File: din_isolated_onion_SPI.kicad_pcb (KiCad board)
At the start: 2 copper layers, 32.5 x 40.5 mm, 17 parts, among them J1 Conn_01x16, J2 Conn_01x16, J3 Conn_01x10, U1 Omega2+, U2 SI8661AB-B-IS1

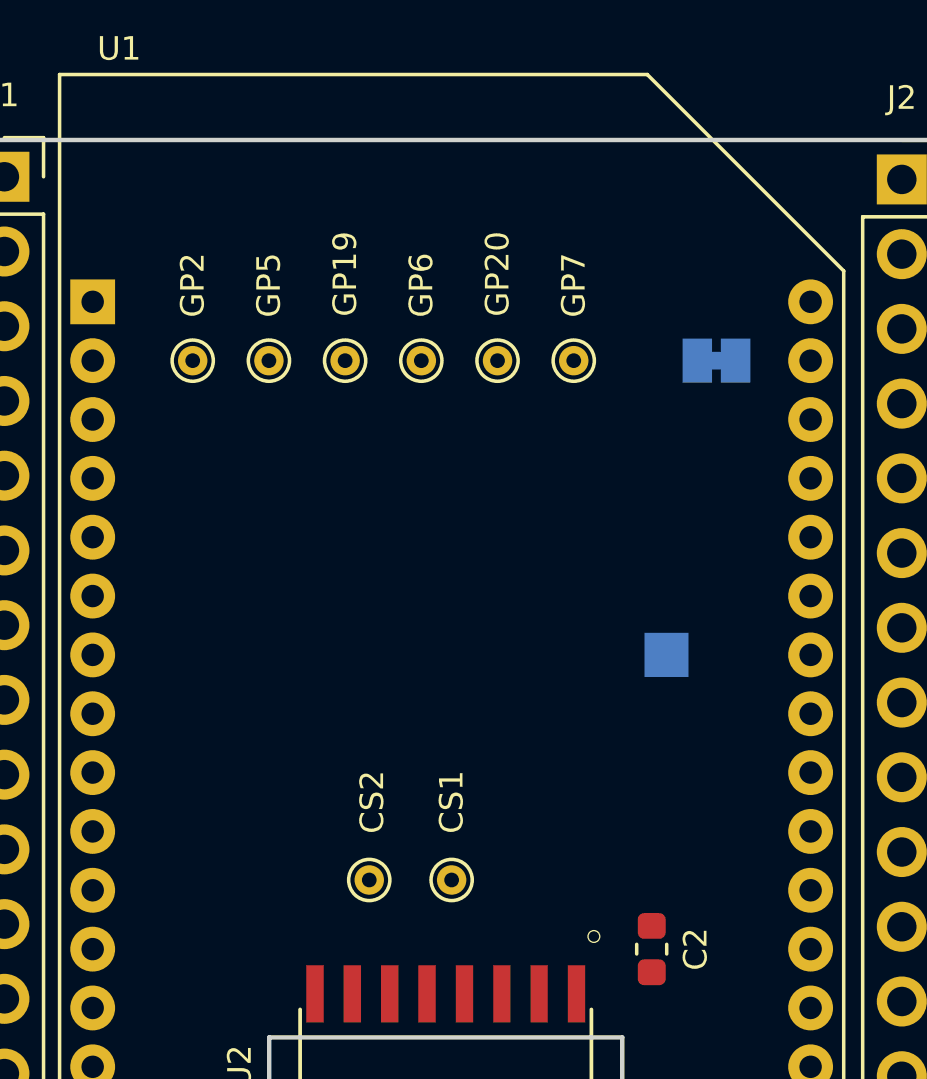
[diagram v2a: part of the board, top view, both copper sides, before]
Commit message: Add reset IC and finalize test points
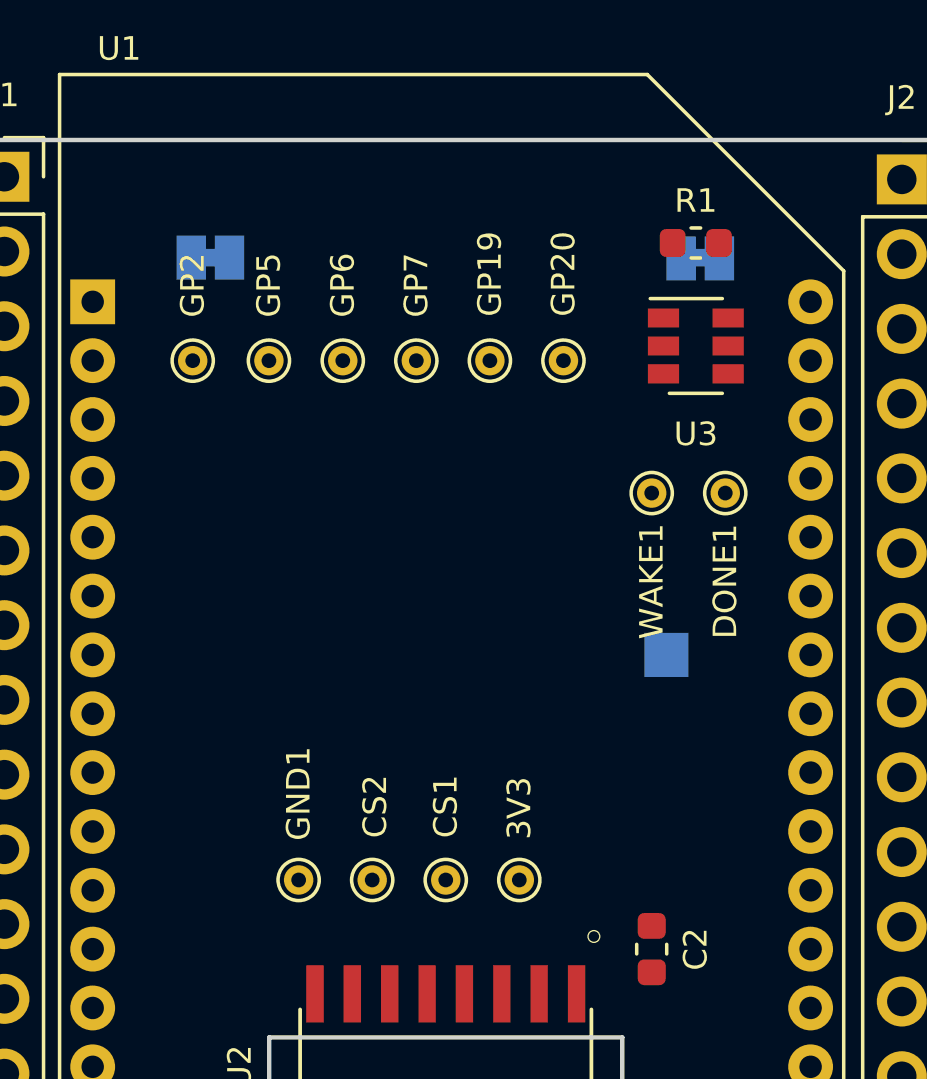
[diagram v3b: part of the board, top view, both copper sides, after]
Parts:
- removed JP1: Jumper_2_Bridged, Jumper:SolderJumper-2_P1.3mm_Bridged_Pad1.0x1.5mm
- added 3V3: TestPoint, TestPoint:TestPoint_THTPad_D1.0mm_Drill0.5mm, F.Cu at (148.5, 104.7)
- added DONE1: TestPoint, TestPoint:TestPoint_THTPad_D1.0mm_Drill0.5mm, F.Cu at (155.5, 91.5)
- added GND1: GND, TestPoint:TestPoint_THTPad_D1.0mm_Drill0.5mm, F.Cu at (141.0, 104.7)
- added LOGO1: Logo_Open_Hardware_Large, Symbol:OSHW-Logo2_7.3x6mm_SilkScreen, B.Cu at (145.0, 100.0)
- added R1: 29.4K, Resistor_SMD:R_0603_1608Metric, F.Cu at (154.5, 83.0)
- added RST1: Jumper_2_Bridged, Jumper:SolderJumper-2_P1.3mm_Bridged_Pad1.0x1.5mm, B.Cu at (154.7, 83.5)
- added U3: TPL5010-Q1, Package_TO_SOT_SMD:SOT-23-6, F.Cu at (154.5, 86.5)
- added VCC1: Jumper_2_Bridged, Jumper:SolderJumper-2_P1.3mm_Bridged_Pad1.0x1.5mm, B.Cu at (138.0, 83.5)
- added WAKE1: TestPoint, TestPoint:TestPoint_THTPad_D1.0mm_Drill0.5mm, F.Cu at (153.0, 91.5)
- CS1: value TestPoint -> ChipSel1
- CS2: value TestPoint -> ChipSel2
- moved GP7 5.35 mm to (145.0, 87.0)
- moved GP19 4.92 mm to (147.5, 87.0)
- moved GP6 2.67 mm to (142.5, 87.0)
- moved GP20 2.24 mm to (150.0, 87.0)
- moved CS1 0.20 mm to (146.0, 104.7)
- moved CS2 0.10 mm to (143.5, 104.7)
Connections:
- net Net-(J2-Pad1) renamed ~RST
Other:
- board text added: "DIN Onion SPI Isolator http://whatnick.com v0.1 2019-06-20"

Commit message: Finalize v0.1 routing
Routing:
- net 3V3_C: track 0.00 -> 103.7 mm, vias 0 -> 1
- net GND_C: track 0.00 -> 94.3 mm, vias 0 -> 5
- net Net-(GP19-Pad1): track 0.00 -> 76.1 mm, vias 0 -> 1
- net Net-(GP20-Pad1): track 0.00 -> 73.2 mm
- net Net-(J2-Pad6): track 0.00 -> 59.4 mm
- net Net-(J2-Pad7): track 0.00 -> 58.4 mm, vias 0 -> 1
- net ~RST: track 0.00 -> 51.4 mm
- net 3V3_O: track 0.00 -> 46.0 mm
- net GND_I: track 0.00 -> 31.8 mm, vias 0 -> 1
- net 3V3_I: track 0.00 -> 31.7 mm
- net CS0_O: track 0.00 -> 20.6 mm
- net CLK_O: track 0.00 -> 20.3 mm
- net Net-(GP7-Pad1): track 0.00 -> 20.3 mm
- net Net-(GP6-Pad1): track 0.00 -> 17.2 mm
- net MOSI_O: track 0.00 -> 16.4 mm, vias 0 -> 1
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- added copper zone on B.Cu, net GND_C
- added copper zone on F.Cu, net GND_C
- added copper zone on B.Cu, net GND_I
- added copper zone on F.Cu, net GND_I

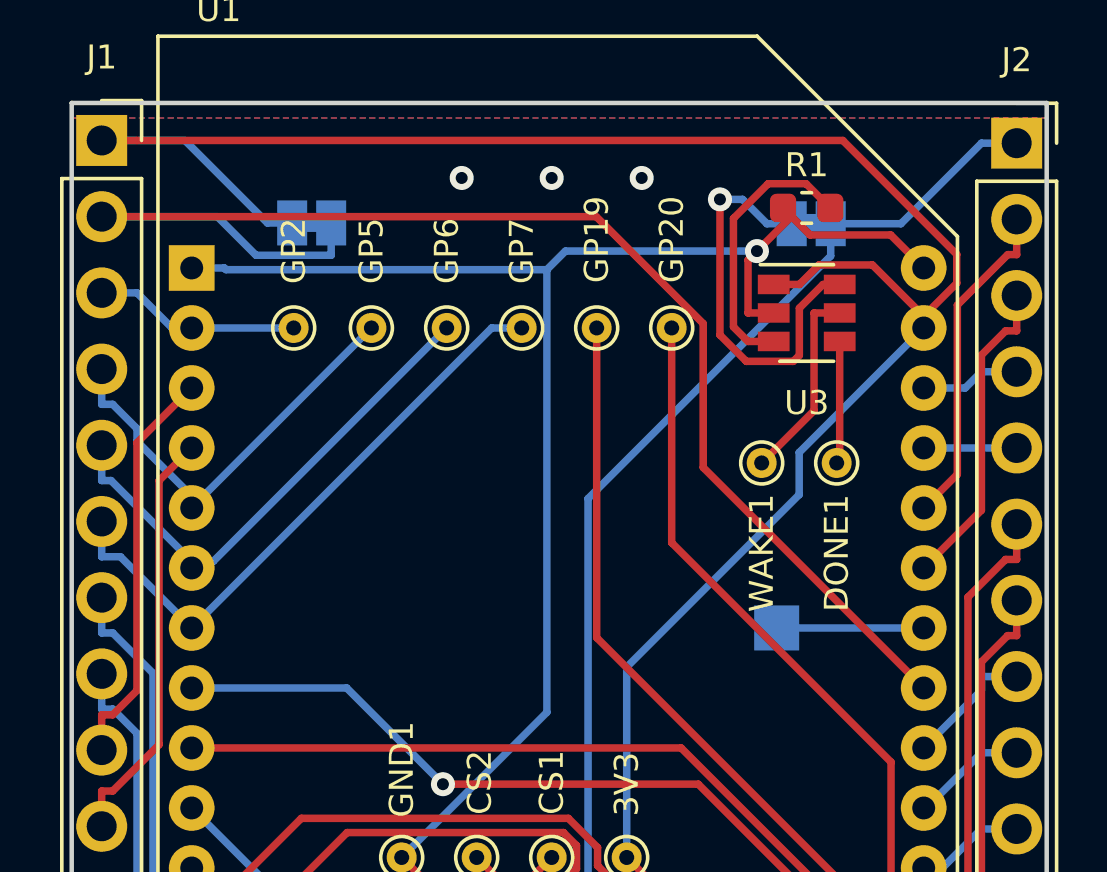
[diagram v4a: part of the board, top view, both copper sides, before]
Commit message: Switch to TSOT for hardware reset
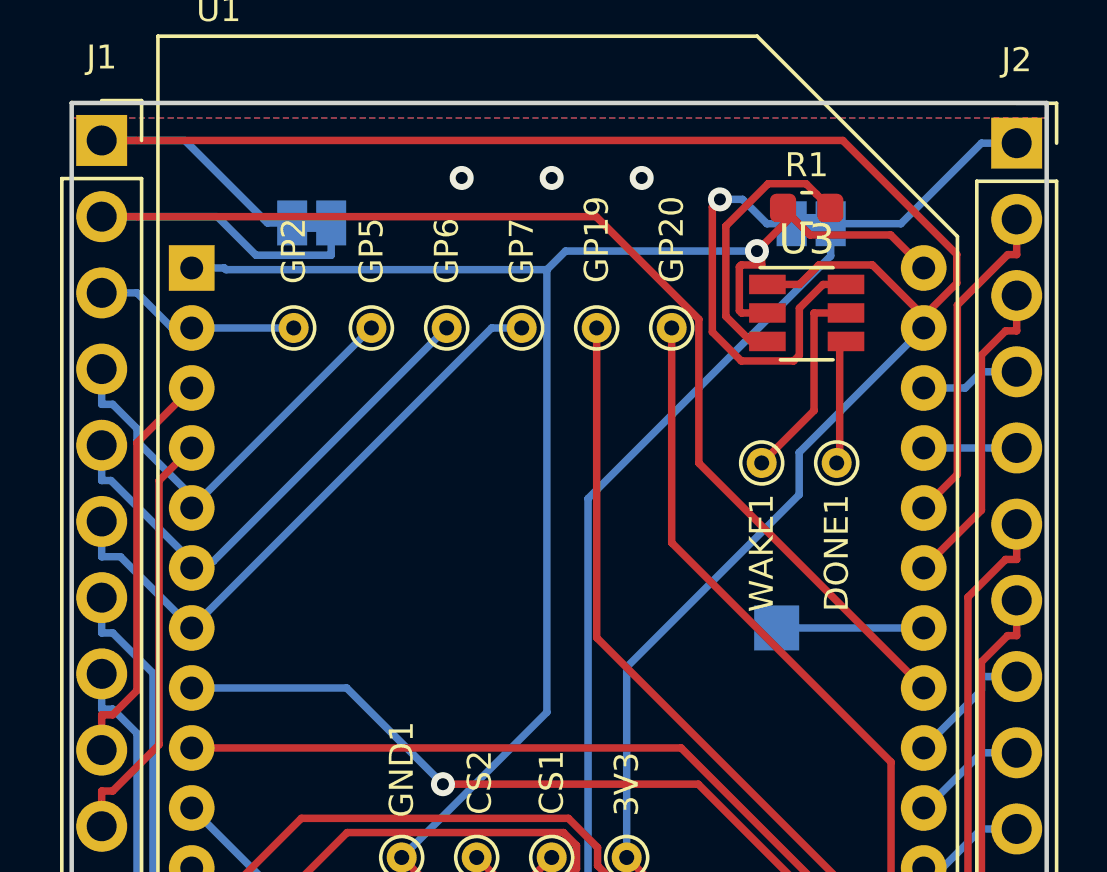
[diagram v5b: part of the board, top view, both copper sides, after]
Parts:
- C1, C2: value C_Small -> 100nF
- U3: footprint Package_TO_SOT_SMD:SOT-23-6 -> Package_TO_SOT_SMD:TSOT-23-6
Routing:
- net GND_C: track 94.3 -> 95.4 mm

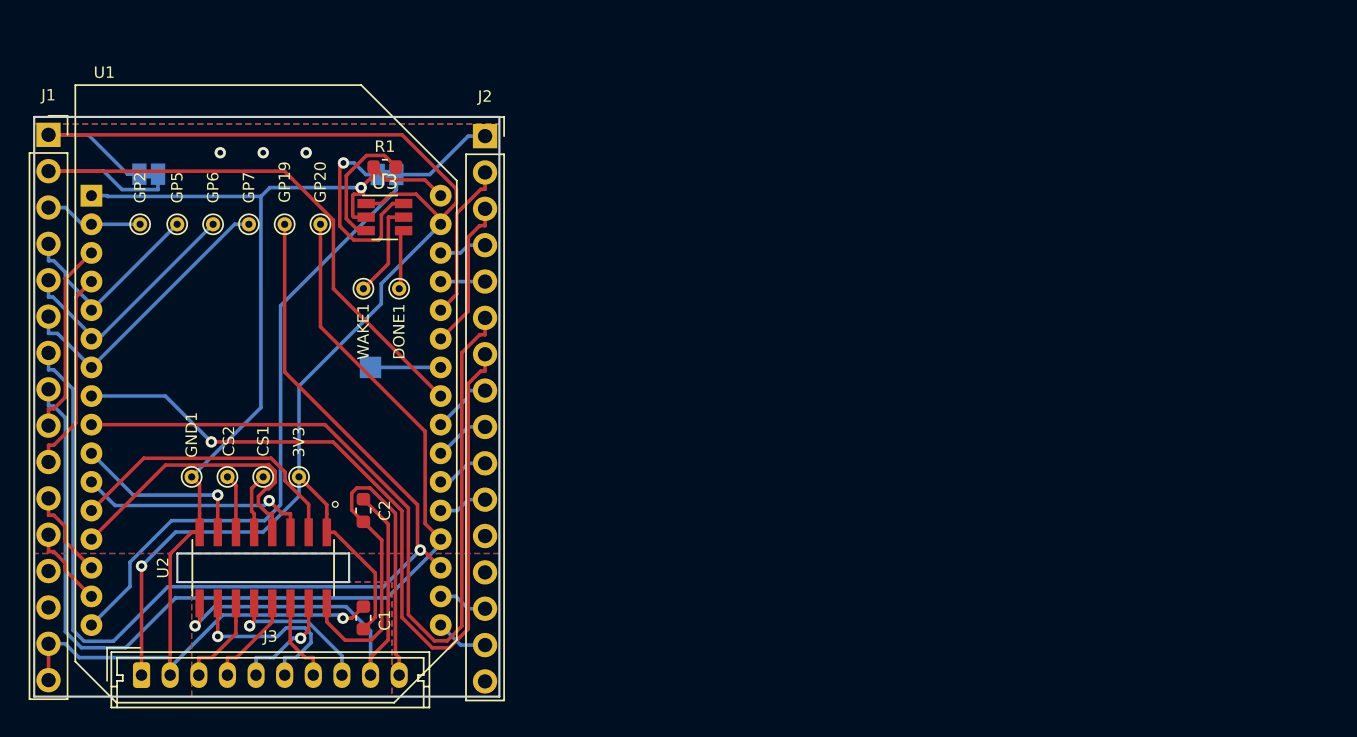
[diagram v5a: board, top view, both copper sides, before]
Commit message: Add quad buffer and GPIO LED's
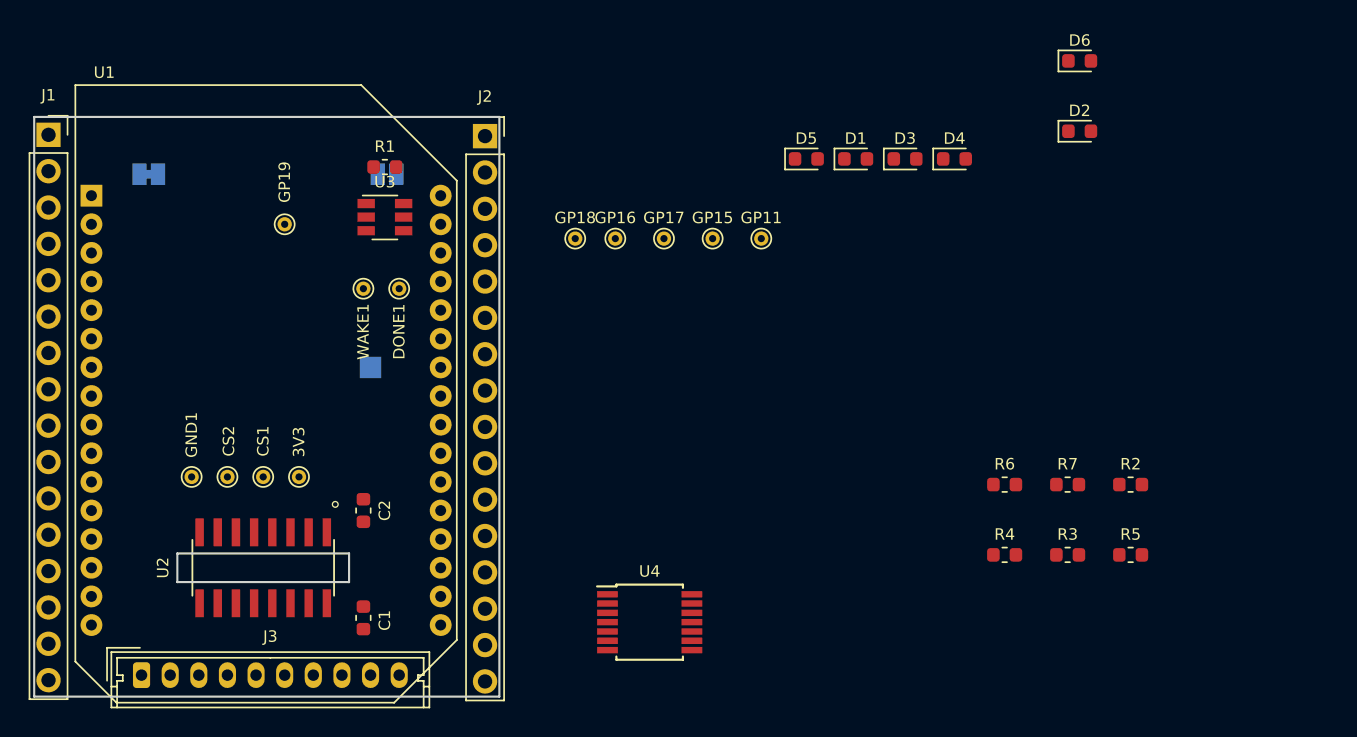
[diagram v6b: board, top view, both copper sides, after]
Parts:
- removed GP2, GP20, GP5, GP6, GP7: TestPoint, TestPoint:TestPoint_THTPad_D1.0mm_Drill0.5mm
- added D1: LED, LED_SMD:LED_0603_1608Metric, F.Cu at (187.4, 82.4)
- added D2: LED, LED_SMD:LED_0603_1608Metric, F.Cu at (203.0, 80.5)
- added D3: LED, LED_SMD:LED_0603_1608Metric, F.Cu at (190.8, 82.4)
- added D4: LED, LED_SMD:LED_0603_1608Metric, F.Cu at (194.3, 82.4)
- added D5: LED, LED_SMD:LED_0603_1608Metric, F.Cu at (183.9, 82.4)
- added D6: LED, LED_SMD:LED_0603_1608Metric, F.Cu at (203.0, 75.6)
- added GP11: TestPoint, TestPoint:TestPoint_THTPad_D1.0mm_Drill0.5mm, F.Cu at (180.8, 88.0)
- added GP15: TestPoint, TestPoint:TestPoint_THTPad_D1.0mm_Drill0.5mm, F.Cu at (177.4, 88.0)
- added GP16: TestPoint, TestPoint:TestPoint_THTPad_D1.0mm_Drill0.5mm, F.Cu at (170.6, 88.0)
- added GP17: TestPoint, TestPoint:TestPoint_THTPad_D1.0mm_Drill0.5mm, F.Cu at (174.0, 88.0)
- added GP18: TestPoint, TestPoint:TestPoint_THTPad_D1.0mm_Drill0.5mm, F.Cu at (167.8, 88.0)
- added R2: 330R, Resistor_SMD:R_0603_1608Metric, F.Cu at (206.6, 105.2)
- added R3: 330R, Resistor_SMD:R_0603_1608Metric, F.Cu at (202.2, 110.1)
- added R4: 330R, Resistor_SMD:R_0603_1608Metric, F.Cu at (197.8, 110.1)
- added R5: 330R, Resistor_SMD:R_0603_1608Metric, F.Cu at (206.6, 110.1)
- added R6: 330R, Resistor_SMD:R_0603_1608Metric, F.Cu at (197.8, 105.2)
- added R7: 330R, Resistor_SMD:R_0603_1608Metric, F.Cu at (202.2, 105.2)
- added U4: 74LVC125, Package_SO:TSSOP-14_4.4x5mm_P0.65mm, F.Cu at (173.0, 114.8)
- RST1: value Jumper_2_Bridged -> Jumper_2_Open; footprint Jumper:SolderJumper-2_P1.3mm_Bridged_Pad1.0x1.5mm -> Jumper:SolderJumper-2_P1.3mm_Open_Pad1.0x1.5mm
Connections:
- net Net-(GP19-Pad1) renamed /GP19
- net Net-(GP2-Pad1) renamed /GP11
- net Net-(GP20-Pad1) renamed /GP18
- net Net-(GP5-Pad1) renamed /GP17
- net Net-(GP6-Pad1) renamed /GP16
- net Net-(GP7-Pad1) renamed /GP15
- U2 pad 7: MISO_O -> MISO_O_ISO
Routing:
- net 3V3_C: track 103.7 -> 0.00 mm, vias 1 -> 0
- net GND_C: track 95.4 -> 0.00 mm, vias 5 -> 0
- net /GP19: track 76.1 -> 0.00 mm, vias 1 -> 0
- net /GP18: track 73.2 -> 0.00 mm
- net Net-(J2-Pad6): track 59.4 -> 0.00 mm
- net Net-(J2-Pad7): track 58.4 -> 0.00 mm, vias 1 -> 0
- net ~RST: track 51.4 -> 0.00 mm
- net 3V3_O: track 46.0 -> 0.00 mm
- net GND_I: track 31.8 -> 0.00 mm, vias 1 -> 0
- net 3V3_I: track 31.7 -> 0.00 mm
- net CS0_O: track 20.6 -> 0.00 mm
- net CLK_O: track 20.3 -> 0.00 mm
- net /GP15: track 20.3 -> 0.00 mm
- net /GP16: track 17.2 -> 0.00 mm
- net MOSI_O: track 16.4 -> 0.00 mm, vias 1 -> 0
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- removed copper zone on B.Cu, net GND_C
- removed copper zone on F.Cu, net GND_C
- removed copper zone on B.Cu, net GND_I
- removed copper zone on F.Cu, net GND_I

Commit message: Move parts into place on PCB for route
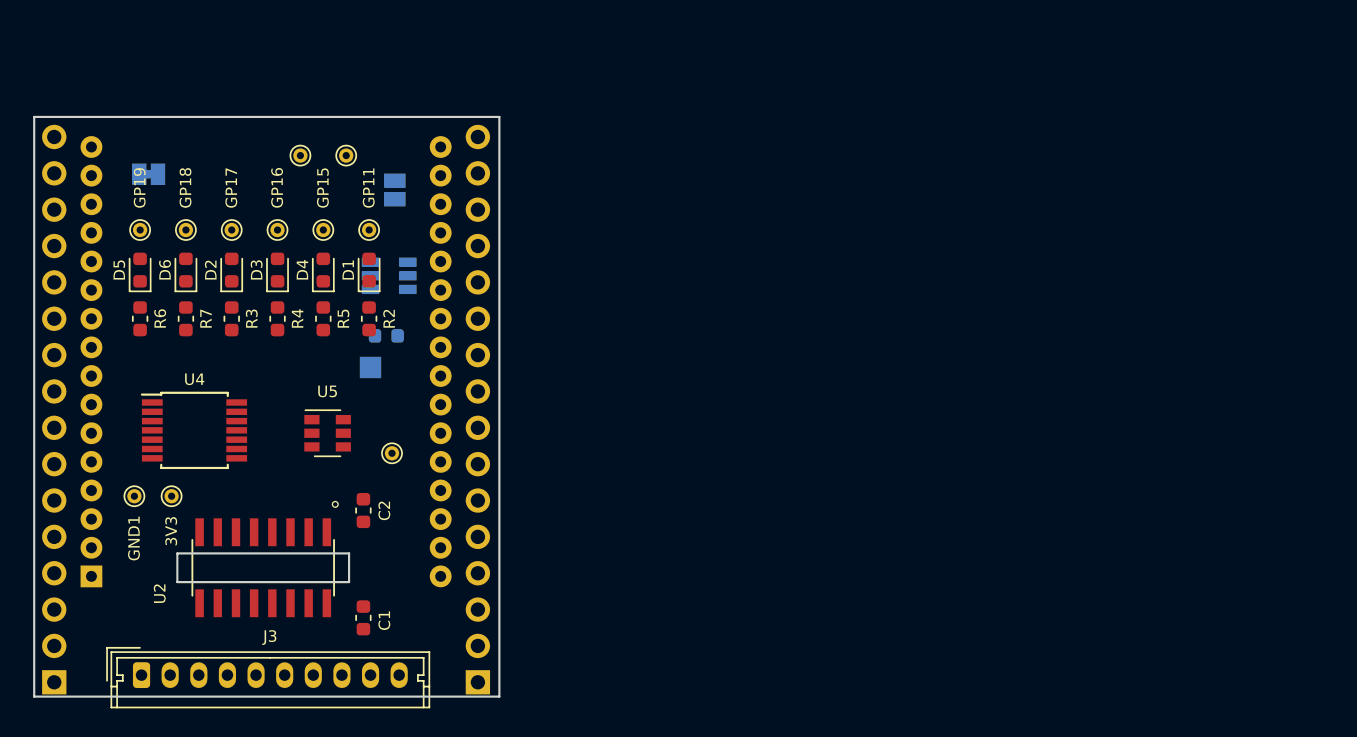
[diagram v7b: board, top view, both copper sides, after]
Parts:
- removed CS1: ChipSel1, TestPoint:TestPoint_THTPad_D1.0mm_Drill0.5mm
- removed CS2: ChipSel2, TestPoint:TestPoint_THTPad_D1.0mm_Drill0.5mm
- added MET_SEL1: MET_S, TestPoint:TestPoint_THTPad_D1.0mm_Drill0.5mm, F.Cu at (155.0, 103.0)
- added U5: NL7SZ19, Package_TO_SOT_SMD:SOT-23-6, F.Cu at (150.5, 101.6)
- J1, J2, R1, U1, U3: moved to B.Cu
- moved D6 64.1 mm to (140.6, 90.2), turned to 90 degrees
- moved R7 62.7 mm to (140.6, 93.6), turned to 270 degrees
- moved R6 61.5 mm to (137.4, 93.6), turned to 270 degrees
- moved R3 60.7 mm to (143.8, 93.6), turned to 270 degrees
- moved D2 60.0 mm to (143.8, 90.2), turned to 90 degrees
- moved R5 58.8 mm to (150.2, 93.6), turned to 270 degrees
- moved R2 54.5 mm to (153.4, 93.6), turned to 270 degrees
- moved R4 53.4 mm to (147.0, 93.6), turned to 270 degrees
- moved D5 47.2 mm to (137.4, 90.2), turned to 90 degrees
- moved D4 44.8 mm to (150.2, 90.2), turned to 90 degrees
- moved D3 44.5 mm to (147.0, 90.2), turned to 90 degrees
- moved J1 38.3 mm to (131.4, 119.0)
- moved J2 38.2 mm to (161.0, 119.0)
- moved D1 34.9 mm to (153.4, 90.2), turned to 90 degrees
- moved U4 34.5 mm to (141.2, 101.4)
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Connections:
- U2 pad 4: CS0_O -> CSMUX_0
- U2 pad 5: CS1_O -> CSMUX_1
- U2 pad 6: CS2_O -> CS_SPARE
